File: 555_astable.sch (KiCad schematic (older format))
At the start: 7 parts, among them U2 555

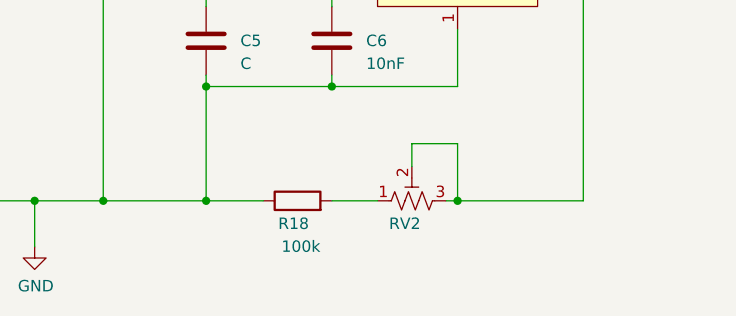
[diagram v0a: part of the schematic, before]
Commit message: Fixed button layout
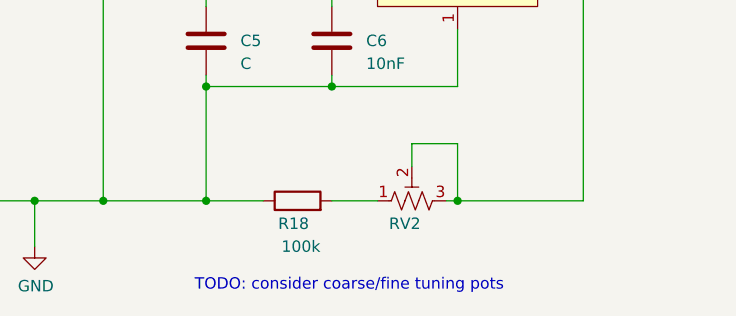
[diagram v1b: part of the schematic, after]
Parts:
- U2: footprint digikey-footprints:DIP-8_W7.62mm -> Package_DIP:DIP-8_W7.62mm
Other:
- note added: "TODO: consider coarse/fine tuning pots"
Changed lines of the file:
@@
 F 0 "U2" H 5800 4050 60  0000 C CNN
 F 1 "555" H 6000 4050 60  0000 C CNN
-F 2 "digikey-footprints:DIP-8_W7.62mm" H 5900 3950 60  0001 L CNN
+F 2 "Package_DIP:DIP-8_W7.62mm" H 5900 3950 60  0001 L CNN
 F 3 "http://www.ti.com/general/docs/suppproductinfo.tsp?distId=10&gotoUrl=http%3A%2F%2Fwww.ti.com%2Flit%2Fgpn%2Fne555" H 5900 4050 60  0001 L CNN
 F 4 "296-1411-5-ND" H 5900 4150 60  0001 L CNN "Digi-Key_PN"
@@
 Wire Wire Line
 	4600 4900 4850 4900
+Text Notes 4550 5300 0    50   ~ 0
+TODO: consider coarse/fine tuning pots
 $EndSCHEMATC

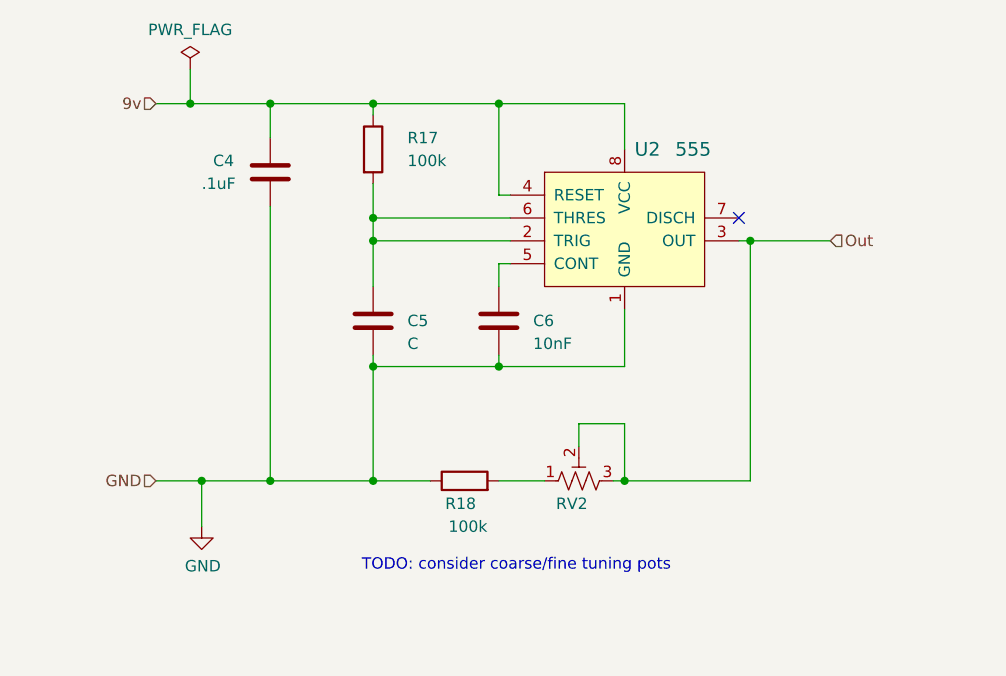
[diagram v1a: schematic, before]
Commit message: Portrait layout, LEDs
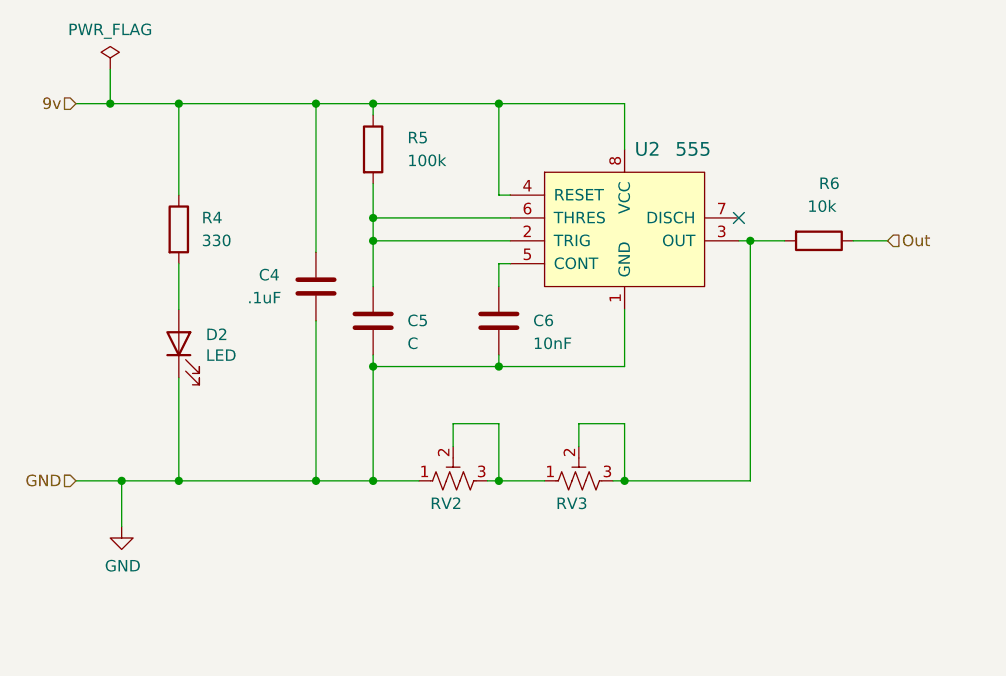
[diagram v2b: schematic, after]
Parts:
- removed R18: 100k, Resistor_THT:R_Axial_DIN0204_L3.6mm_D1.6mm_P7.62mm_Horizontal, symbol Device:R
- added D2: LED, LED_THT:LED_D3.0mm, symbol Device:LED
- added R4: 330, Resistor_THT:R_Axial_DIN0207_L6.3mm_D2.5mm_P2.54mm_Vertical, symbol Device:R
- added R6: 10k, Resistor_THT:R_Axial_DIN0204_L3.6mm_D1.6mm_P7.62mm_Horizontal, symbol Device:R
- added RV2: R_POT_TRIM_US, Potentiometer_THT:Potentiometer_Bourns_3296W_Vertical, symbol Device:R_POT_TRIM_US
- C4, C5, C6: footprint Capacitor_THT:C_Axial_L3.8mm_D2.6mm_P7.50mm_Horizontal -> Capacitor_THT:C_Disc_D5.0mm_W2.5mm_P5.00mm
- RV3: renamed from RV2; footprint Potentiometer_THT:Potentiometer_Bourns_3296W_Vertical -> Potentiometer_THT:Potentiometer_Bourns_3386F_Vertical
- renumbered R17 to R5
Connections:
- net 9v: now also R4.1
- net GND: now also D2.1 (K), RV2.1
- net Out: now also R6.1; no longer RV3.2, RV3.3, U2.3 (OUT)
- net at RV3.1: now also RV2.2, RV2.3
- new net: R6.2, RV3.2, RV3.3, U2.3 (OUT)
- new net: D2.2 (A), R4.2
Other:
- note removed: "TODO: consider coarse/fine tuning pots"
- moved on the sheet: C4

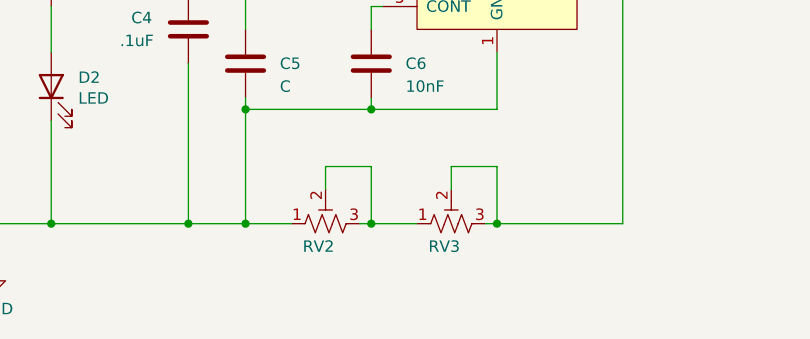
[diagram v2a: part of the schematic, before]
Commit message: Mounting holes
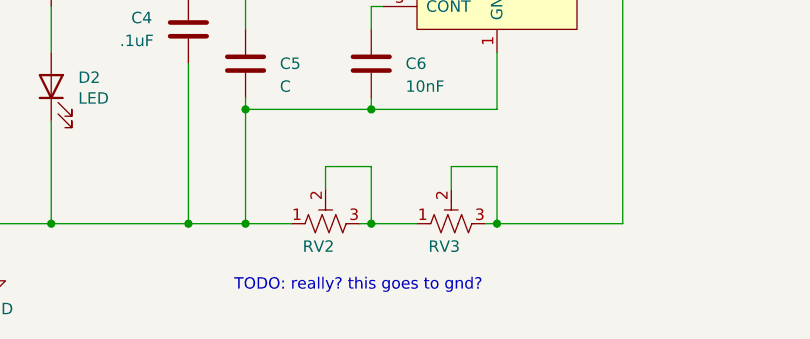
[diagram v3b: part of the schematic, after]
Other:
- note added: "TODO: really? this goes to gnd?"
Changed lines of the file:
@@
 	5150 4900 5350 4900
 Connection ~ 5150 4900
+Text Notes 4550 5200 0    50   ~ 0
+TODO: really? this goes to gnd?
 $EndSCHEMATC

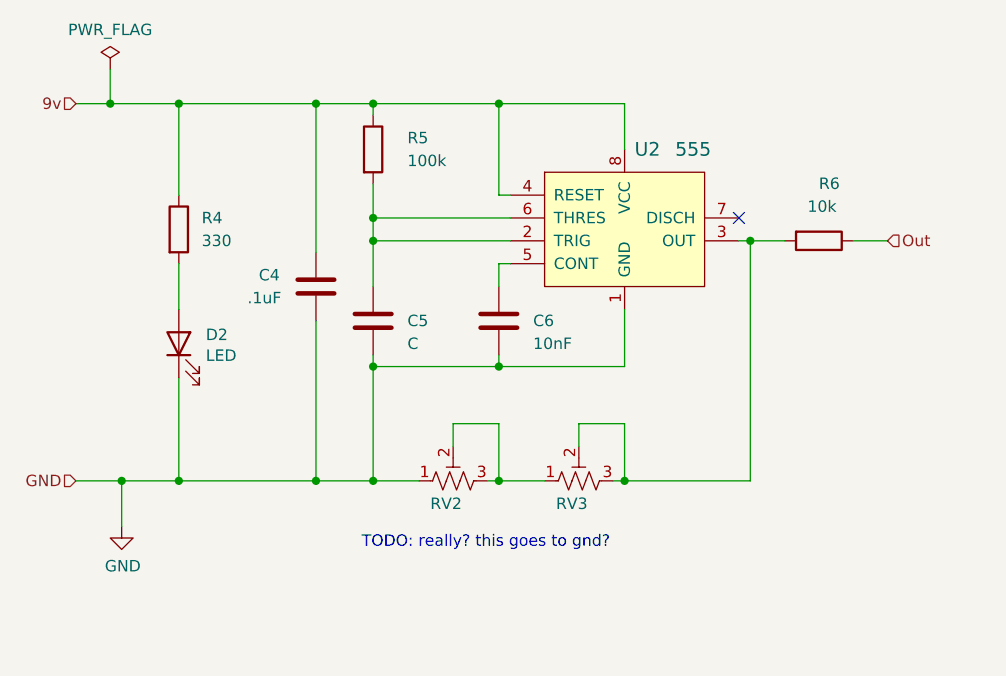
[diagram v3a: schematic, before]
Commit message: Rerouting after footpring changes
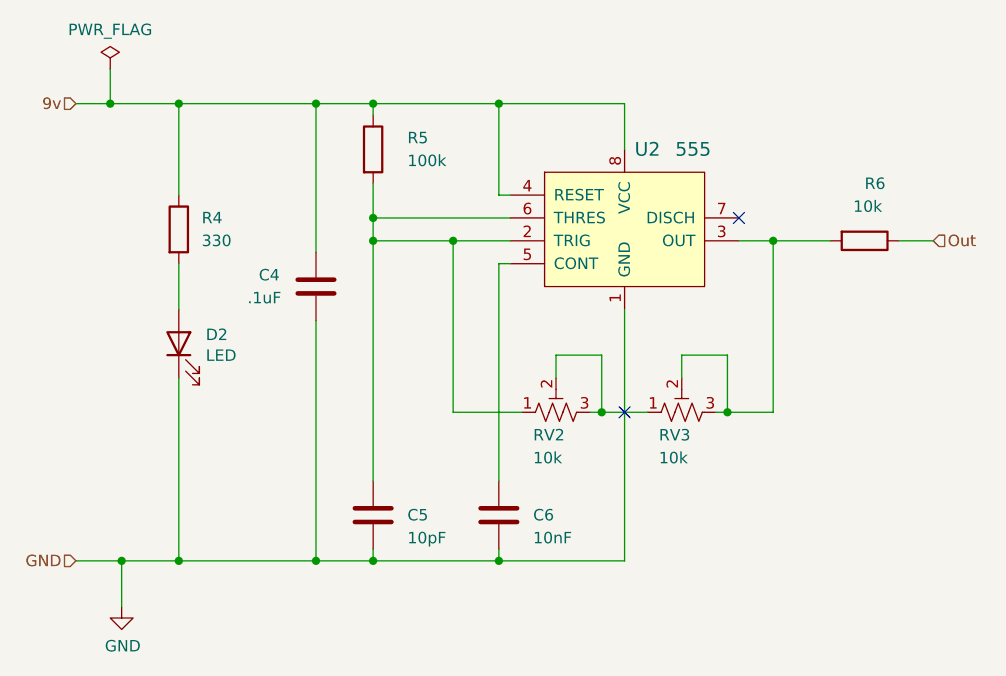
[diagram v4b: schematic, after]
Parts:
- C5: value C -> 10pF
- RV2, RV3: value R_POT_TRIM_US -> 10k
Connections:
- net GND: no longer RV2.1
- net at C5.1, R5.2, U2.2 (TRIG)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: now also RV2.1
- no-connect marks 1 -> 2
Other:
- note removed: "TODO: really? this goes to gnd?"
- moved on the sheet: C5, C6, R6, RV2, RV3

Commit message: Whoa! Key-to-555 tracks visible as silkscreen
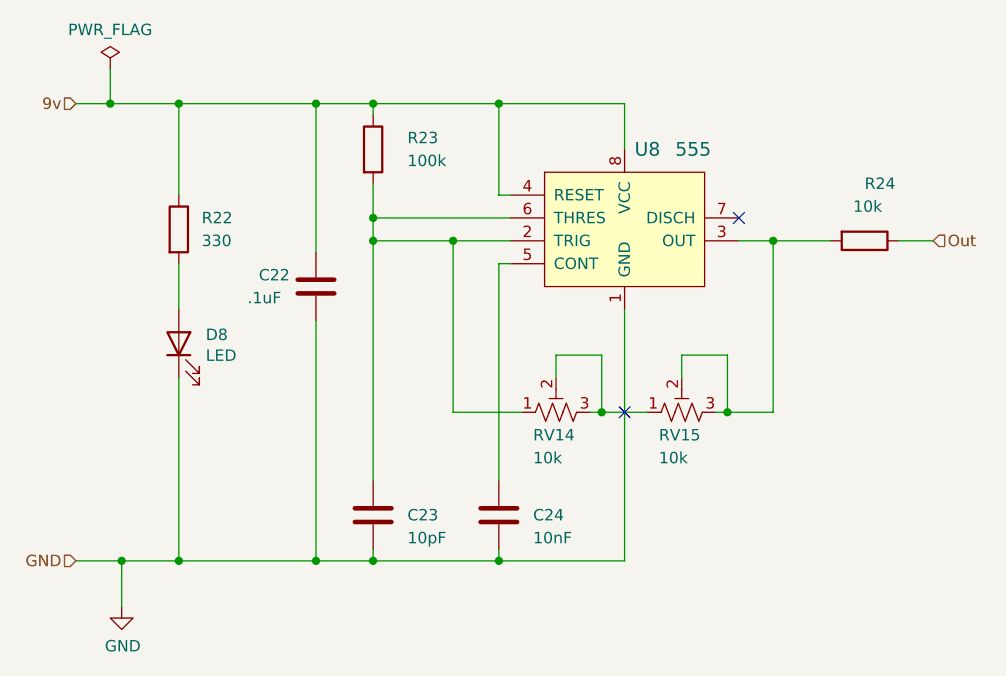
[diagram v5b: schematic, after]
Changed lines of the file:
@@
 $Descr A4 11693 8268
 encoding utf-8
-Sheet 2 14
+Sheet 8 14
 Title ""
 Date ""
@@
 AR Path="/5EF6060B/60F6A68E" Ref="R38"  Part="1"
 AR Path="/5EF7A07F/60F6A68E" Ref="R41"  Part="1"
-F 0 "R5" H 4750 3500 50  0000 L CNN
+F 0 "R23" H 4750 3500 50  0000 L CNN
 F 1 "100k" H 4750 3400 50  0000 L CNN
 F 2 "Resistor_THT:R_Axial_DIN0204_L3.6mm_D1.6mm_P7.62mm_Horizontal" V 4530 3450 50  0001 C CNN
@@
 AR Path="/5EF6060B/60F6EAC0" Ref="C37"  Part="1"
 AR Path="/5EF7A07F/60F6EAC0" Ref="C40"  Part="1"
-F 0 "C4" H 4100 4100 50  0000 L CNN
+F 0 "C22" H 4100 4100 50  0000 L CNN
 F 1 ".1uF" H 4050 4000 50  0000 L CNN
 F 2 "Capacitor_THT:C_Disc_D5.0mm_W2.5mm_P5.00mm" H 4388 3900 50  0001 C CNN
@@
 AR Path="/5EF6060B/60F6A6DA" Ref="U13"  Part="1"
 AR Path="/5EF7A07F/60F6A6DA" Ref="U14"  Part="1"
-F 0 "U2" H 5800 4050 60  0000 C CNN
+F 0 "U8" H 5800 4050 60  0000 C CNN
 F 1 "555" H 6000 4050 60  0000 C CNN
 F 2 "Package_DIP:DIP-8_W7.62mm" H 5900 3950 60  0001 L CNN
@@
 AR Path="/5EF6060B/60F6A6C5" Ref="RV25"  Part="1"
 AR Path="/5EF7A07F/60F6A6C5" Ref="RV27"  Part="1"
-F 0 "RV3" V 5850 4700 50  0000 R CNN
+F 0 "RV15" V 5850 4700 50  0000 R CNN
 F 1 "10k" V 5750 4700 50  0000 R CNN
 F 2 "Potentiometer_THT:Potentiometer_Bourns_3386F_Vertical" H 5950 4600 50  0001 C CNN
@@
 AR Path="/5EF6060B/5EFAE830" Ref="R39"  Part="1"
 AR Path="/5EF7A07F/5EFAE830" Ref="R42"  Part="1"
-F 0 "R6" V 6500 3850 50  0000 L CNN
+F 0 "R24" V 6500 3850 50  0000 L CNN
 F 1 "10k" V 6600 3800 50  0000 L CNN
 F 2 "Resistor_THT:R_Axial_DIN0204_L3.6mm_D1.6mm_P7.62mm_Horizontal" V 6680 3850 50  0001 C CNN
@@
 AR Path="/5EF6060B/5F127BEF" Ref="D13"  Part="1"
 AR Path="/5EF7A07F/5F127BEF" Ref="D14"  Part="1"
-F 0 "D2" V 3789 4182 50  0000 R CNN
+F 0 "D8" V 3789 4182 50  0000 R CNN
 F 1 "LED" V 3698 4182 50  0000 R CNN
 F 2 "LED_THT:LED_D3.0mm" H 3750 4300 50  0001 C CNN
@@
 AR Path="/5EF6060B/5F127BF5" Ref="R37"  Part="1"
 AR Path="/5EF7A07F/5F127BF5" Ref="R40"  Part="1"
-F 0 "R4" H 3850 3850 50  0000 L CNN
+F 0 "R22" H 3850 3850 50  0000 L CNN
 F 1 "330" H 3850 3750 50  0000 L CNN
 F 2 "Resistor_THT:R_Axial_DIN0207_L6.3mm_D2.5mm_P2.54mm_Vertical" V 3680 3800 50  0001 C CNN
@@
 AR Path="/5EF6060B/5F13ACF1" Ref="RV24"  Part="1"
 AR Path="/5EF7A07F/5F13ACF1" Ref="RV26"  Part="1"
-F 0 "RV2" V 5300 4700 50  0000 R CNN
+F 0 "RV14" V 5300 4700 50  0000 R CNN
 F 1 "10k" V 5200 4700 50  0000 R CNN
 F 2 "Potentiometer_THT:Potentiometer_Bourns_3296W_Vertical" H 5400 4600 50  0001 C CNN
@@
 AR Path="/5EF6060B/60F6A6A0" Ref="C39"  Part="1"
 AR Path="/5EF7A07F/60F6A6A0" Ref="C42"  Part="1"
-F 0 "C6" H 5300 5050 50  0000 L CNN
+F 0 "C24" H 5300 5050 50  0000 L CNN
 F 1 "10nF" H 5300 4950 50  0000 L CNN
 F 2 "Capacitor_THT:C_Disc_D5.0mm_W2.5mm_P5.00mm" H 5188 4900 50  0001 C CNN
@@
 AR Path="/5EF6060B/60F6A69A" Ref="C38"  Part="1"
 AR Path="/5EF7A07F/60F6A69A" Ref="C41"  Part="1"
-F 0 "C5" H 4750 5050 50  0000 L CNN
+F 0 "C23" H 4750 5050 50  0000 L CNN
 F 1 "10pF" H 4750 4950 50  0000 L CNN
 F 2 "Capacitor_THT:C_Disc_D5.0mm_W2.5mm_P5.00mm" H 4638 4900 50  0001 C CNN
